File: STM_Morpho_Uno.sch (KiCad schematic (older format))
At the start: 6 parts, among them CN10 Conn_02x19_Odd_Even, CN5 Conn_01x10_Female, CN6 Conn_01x08_Female, CN7 Conn_02x19_Odd_Even, CN8 Conn_01x06_Female, CN9 Conn_01x08_Female

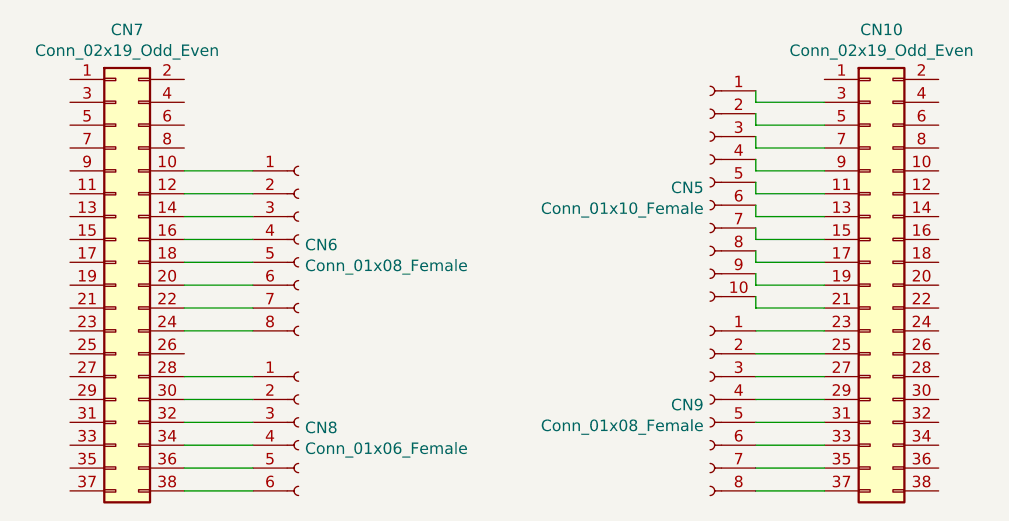
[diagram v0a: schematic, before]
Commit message: fix, right uno connector where upside down compared to datasheet
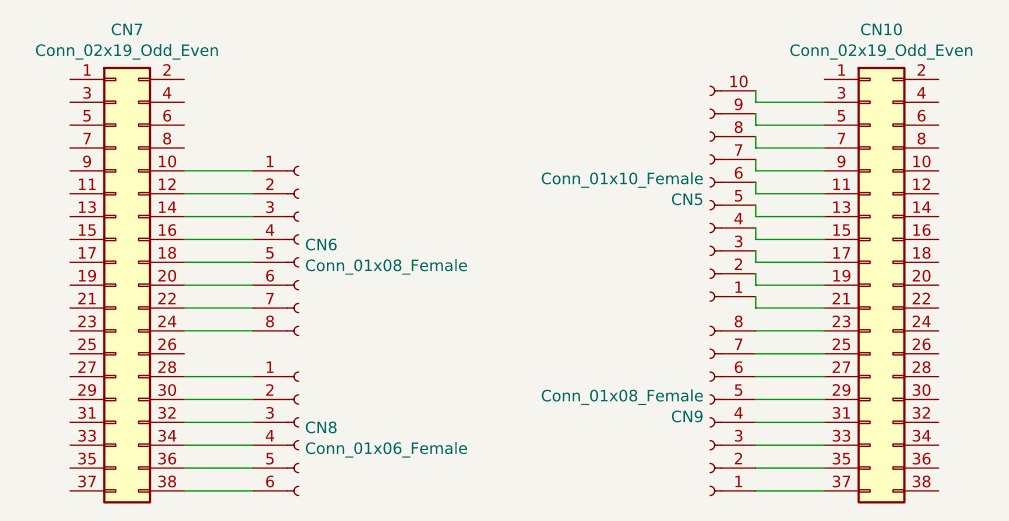
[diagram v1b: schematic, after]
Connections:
- net at CN10.11 (Pin_11): now also CN5.6 (Pin_6); no longer CN5.5 (Pin_5)
- net at CN10.13 (Pin_13): now also CN5.5 (Pin_5); no longer CN5.6 (Pin_6)
- net at CN10.15 (Pin_15): now also CN5.4 (Pin_4); no longer CN5.7 (Pin_7)
- net at CN10.17 (Pin_17): now also CN5.3 (Pin_3); no longer CN5.8 (Pin_8)
- net at CN10.19 (Pin_19): now also CN5.2 (Pin_2); no longer CN5.9 (Pin_9)
- net at CN10.21 (Pin_21): now also CN5.1 (Pin_1); no longer CN5.10 (Pin_10)
- net at CN10.23 (Pin_23): now also CN9.8 (Pin_8); no longer CN9.1 (Pin_1)
- net at CN10.25 (Pin_25): now also CN9.7 (Pin_7); no longer CN9.2 (Pin_2)
- net at CN10.27 (Pin_27): now also CN9.6 (Pin_6); no longer CN9.3 (Pin_3)
- net at CN10.29 (Pin_29): now also CN9.5 (Pin_5); no longer CN9.4 (Pin_4)
- net at CN10.3 (Pin_3): now also CN5.10 (Pin_10); no longer CN5.1 (Pin_1)
- net at CN10.31 (Pin_31): now also CN9.4 (Pin_4); no longer CN9.5 (Pin_5)
- net at CN10.33 (Pin_33): now also CN9.3 (Pin_3); no longer CN9.6 (Pin_6)
- net at CN10.35 (Pin_35): now also CN9.2 (Pin_2); no longer CN9.7 (Pin_7)
- net at CN10.37 (Pin_37): now also CN9.1 (Pin_1); no longer CN9.8 (Pin_8)
- net at CN10.5 (Pin_5): now also CN5.9 (Pin_9); no longer CN5.2 (Pin_2)
- net at CN10.7 (Pin_7): now also CN5.8 (Pin_8); no longer CN5.3 (Pin_3)
- net at CN10.9 (Pin_9): now also CN5.7 (Pin_7); no longer CN5.4 (Pin_4)
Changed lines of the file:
@@
 L Connector:Conn_01x08_Female CN9
 U 1 1 60687881
-P 4500 3700
-F 0 "CN9" H 4528 3676 50  0000 L CNN
-F 1 "Conn_01x08_Female" H 4528 3585 50  0000 L CNN
-F 2 "Connector_PinSocket_2.54mm:PinSocket_1x08_P2.54mm_Vertical" H 4500 3700 50  0001 C CNN
-F 3 "~" H 4500 3700 50  0001 C CNN
-	1    4500 3700
-	-1   0    0    -1
+P 4500 3800
+F 0 "CN9" H 4528 3776 50  0000 L CNN
+F 1 "Conn_01x08_Female" H 4528 3685 50  0000 L CNN
+F 2 "Connector_PinSocket_2.54mm:PinSocket_1x08_P2.54mm_Vertical" H 4500 3800 50  0001 C CNN
+F 3 "~" H 4500 3800 50  0001 C CNN
+	1    4500 3800
+	-1   0    0    1
 $EndComp
 $Comp
@@
 L Connector:Conn_01x10_Female CN5
 U 1 1 60689832
-P 4500 2750
-F 0 "CN5" H 4528 2726 50  0000 L CNN
-F 1 "Conn_01x10_Female" H 4528 2635 50  0000 L CNN
-F 2 "Connector_PinSocket_2.54mm:PinSocket_1x10_P2.54mm_Vertical" H 4500 2750 50  0001 C CNN
-F 3 "~" H 4500 2750 50  0001 C CNN
-	1    4500 2750
-	-1   0    0    -1
+P 4500 2850
+F 0 "CN5" H 4528 2826 50  0000 L CNN
+F 1 "Conn_01x10_Female" H 4528 2735 50  0000 L CNN
+F 2 "Connector_PinSocket_2.54mm:PinSocket_1x10_P2.54mm_Vertical" H 4500 2850 50  0001 C CNN
+F 3 "~" H 4500 2850 50  0001 C CNN
+	1    4500 2850
+	-1   0    0    1
 $EndComp
 Wire Wire Line
